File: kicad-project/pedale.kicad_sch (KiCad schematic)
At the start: 45 parts, among them IC1 TLV76150DCYR, IC2 TLV76150DCYR, IC3 TLV76150DCYR, IC4 TLV76150DCYR, IC5 TLV76150DCYR

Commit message: modificari
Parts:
- U1, U8: footprint Connector_PinHeader_2.54mm:PinHeader_1x02_P2.54mm_Vertical -> Connector_PinSocket_2.00mm:PinSocket_1x02_P2.00mm_Horizontal
- U2, U3, U5, U6, U7: footprint Connector_PinHeader_2.54mm:PinHeader_1x03_P2.54mm_Vertical -> Connector_PinSocket_2.00mm:PinSocket_1x03_P2.00mm_Horizontal
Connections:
- net GND: now also J13.12 (GND), J13.14 (GND)
- net 5V_5: now reaches C10.1, IC4.2 (OUT_1), IC4.4 (OUT_2), U7.1 (5V)
- net 5V_2: now reaches C7.1, IC1.2 (OUT_1), IC1.4 (OUT_2), U2.1 (5V)
- net 12V: now reaches C1.1, C3.1, C4.1, C5.1, C6.1, IC1.3 (IN), IC2.3 (IN), IC3.3 (IN), IC4.3 (IN), IC5.3 (IN), U1.2 (12V), U9.1 (VIN)
- net CAN_P: now reaches U4.3 (CANH), U8.1 (CANH)
- net CAN_N: now reaches U4.2 (CANL), U8.2 (CANL)
- net 5V_1: now reaches C2.1, IC5.2 (OUT_1), IC5.4 (OUT_2), U3.1 (5V)
- net 5V_3: now reaches C8.1, IC2.2 (OUT_1), IC2.4 (OUT_2), U5.1 (5V)
- net 5V_4: now reaches C9.1, IC3.2 (OUT_1), IC3.4 (OUT_2), U6.1 (5V)
- no-connect marks 101 -> 99
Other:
- moved on the sheet: U8

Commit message: Schimbari dupa sugestii noi
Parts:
- removed U9: ~, Connector_PinHeader_2.54mm:PinHeader_1x01_P2.54mm_Vertical, symbol pedale-lib:Conn_J23
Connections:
- net 12V: now also J13.16 (VBAT)
- net GND: no longer J13.12 (GND), J13.14 (GND), J2.7 (GND), J4.10 (GND)
- no-connect marks 99 -> 102

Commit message: modificari aplicate
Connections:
- net GND: now also R0.2, R12.2, R3.2, R6.2, R9.2; no longer R11.2, R14.2, R2.2, R5.2, R8.2
- net at R0.1: now also J14.2 (ptd1), R2.2; no longer U7.3 (A0)
- net at U3.3 (A0): now also R13.1; no longer R12.1
- net at R6.1: now also J14.6 (pta13), R8.2; no longer U5.3 (A0)
- net at R9.1: now also J14.8 (pta8), R11.2; no longer U2.3 (A0)
- net at R3.1: now also J14.4 (ptd0), R5.2; no longer U6.3 (A0)
- new net: J14.10 (pta9), R12.1, R14.2
- new net: R10.1, U2.3 (A0)
- new net: R1.1, U7.3 (A0)
- new net: R7.1, U5.3 (A0)
- new net: R4.1, U6.3 (A0)
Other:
- moved on the sheet: R0, R1, R10, R11, R12, R13, R14, R2, R3, R4, R5, R6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

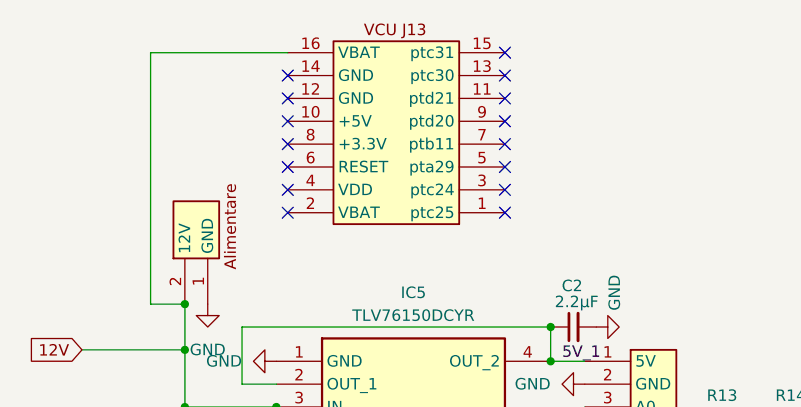
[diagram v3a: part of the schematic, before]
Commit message: trebuie sa verific/schimb conectorii sa aiba pinii buni
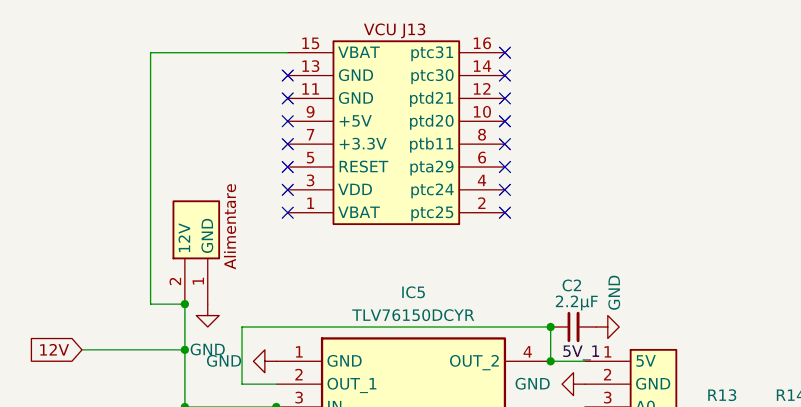
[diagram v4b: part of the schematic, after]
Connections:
- net 12V: now also J13.15 (VBAT); no longer J13.16 (VBAT)
